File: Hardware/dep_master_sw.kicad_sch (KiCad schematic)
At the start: 11 parts, among them Q5 BSZ025N04LS, Q6 BSZ025N04LS, U8 LM74810

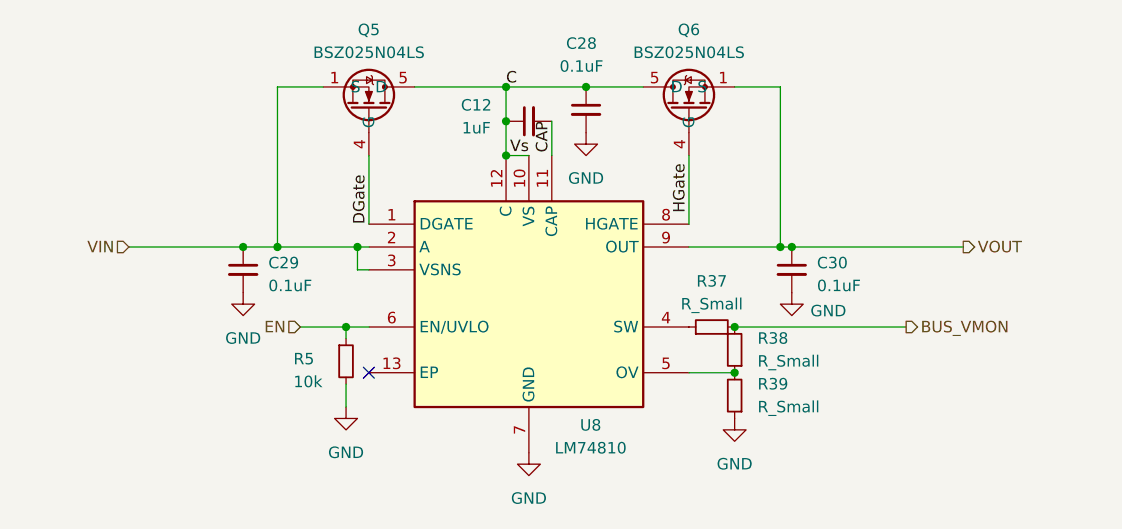
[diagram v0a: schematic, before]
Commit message: TVS diode and sized resistor ladder
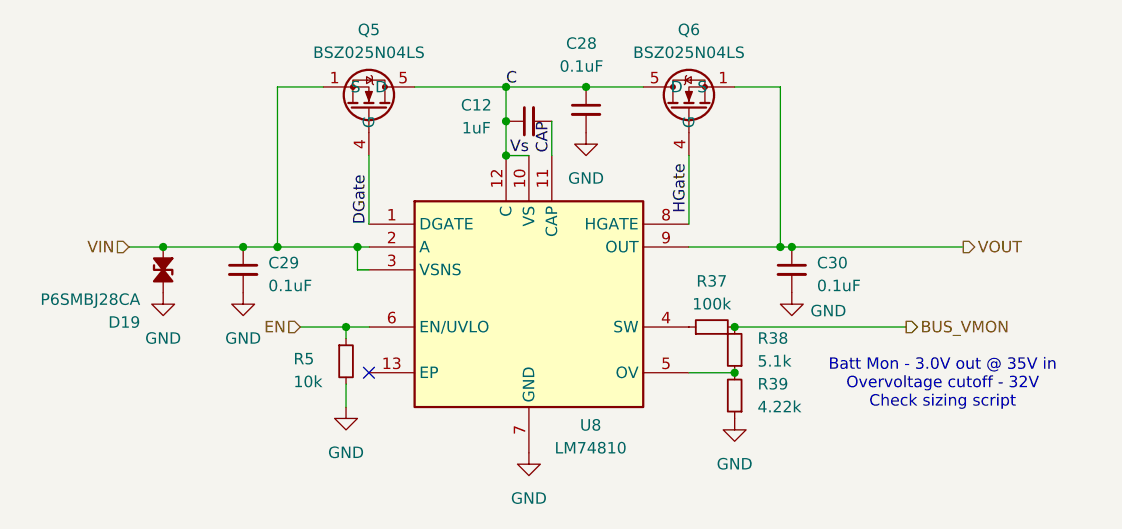
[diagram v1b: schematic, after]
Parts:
- added D19: P6SMBJ28CA, Diode_SMD:D_SMA, symbol Device:D_TVS_Small_Filled
- R37: value R_Small -> 100k
- R38: value R_Small -> 5.1k
- R39: value R_Small -> 4.22k
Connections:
- net GND: now also D19.2 (A2)
- net VIN: now also D19.1 (A1)
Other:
- note added: "Batt Mon - 3.0V out @ 35V in Overvoltage cutoff - 32V Check sizing script"
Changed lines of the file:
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@@
+		(color 0 0 0 0)
+	)
+	(junction
+		(at 99.06 62.23)
+		(diameter 0)
 		(color 0 0 0 0)
 	)
@@
 	(wire
 		(pts
+			(xy 99.06 62.23) (xy 107.95 62.23)
+		)
+		(stroke
+			(width 0)
+			(type default)
+		)
+	)
+	(wire
+		(pts
 			(xy 157.48 52.07) (xy 157.48 59.69)
 		)
@@
 	(wire
 		(pts
-			(xy 95.25 62.23) (xy 107.95 62.23)
+			(xy 95.25 62.23) (xy 99.06 62.23)
 		)
 		(stroke
@@
 			(width 0)
 			(type default)
+		)
+	)
+	(text "Batt Mon - 3.0V out @ 35V in\nOvervoltage cutoff - 32V\nCheck sizing script"
+		(exclude_from_sim no)
+		(at 185.674 77.47 0)
+		(effects
+			(font
+				(size 1.27 1.27)
+			)
 		)
 	)
@@
 	)
 	(symbol
+		(lib_id "power:GND")
+		(at 99.06 67.31 0)
+		(unit 1)
+		(exclude_from_sim no)
+		(in_bom yes)
+		(on_board yes)
+		(dnp no)
+		(fields_autoplaced yes)
+		(property "Reference" "#PWR077"
+			(at 99.06 73.66 0)
+			(effects
+				(font
+					(size 1.27 1.27)
+				)
+				(hide yes)
+			)
+		)
+		(property "Value" "GND"
+			(at 99.06 72.39 0)
+			(effects
+				(font
+					(size 1.27 1.27)
+				)
+			)
+		)
+		(property "Footprint" ""
+			(at 99.06 67.31 0)
+			(effects
+				(font
+					(size 1.27 1.27)
+				)
+				(hide yes)
+			)
+		)
+		(property "Datasheet" ""
+			(at 99.06 67.31 0)
+			(effects
+				(font
+					(size 1.27 1.27)
+				)
+				(hide yes)
+			)
+		)
+		(property "Description" "Power symbol creates a global label with name \"GND\" , ground"
+			(at 99.06 67.31 0)
+			(effects
+				(font
+					(size 1.27 1.27)
+				)
+				(hide yes)
+			)
+		)
+		(pin "1"
+		)
+		(instances
+			(project "flintandsteel"
+				(path "/7db990e4-92e1-4f99-b4d2-435bbec1ba83/62d4ea8d-f53f-40d2-8855-48df78fda698"
+					(reference "#PWR077")
+					(unit 1)
+				)
+			)
+		)
+	)
+	(symbol
 		(lib_id "Device:R_Small")
 		(at 160.02 71.12 90)
@@
 			)
 		)
-		(property "Value" "R_Small"
+		(property "Value" "100k"
 			(at 160.02 68.58 90)
 			(effects
@@
 			)
 		)
-		(property "Value" "R_Small"
+		(property "Value" "5.1k"
 			(at 165.1 74.9299 0)
 			(effects
@@
 			)
 		)
-		(property "Value" "R_Small"
+		(property "Value" "4.22k"
 			(at 165.1 80.0099 0)
 			(effects
@@
 					(unit 1)
 				)
+			)
+		)
+	)
+	(symbol
+		(lib_id "Device:D_TVS_Small_Filled")
+		(at 99.06 64.77 270)
+		(unit 1)
+		(exclude_from_sim no)
+		(in_bom yes)
+		(on_board yes)
+		(dnp no)
+		(property "Reference" "D19"
+			(at 96.52 70.612 90)
+			(effects
+				(font
+					(size 1.27 1.27)
+				)
+				(justify right)
+			)
+		)
+		(property "Value" "P6SMBJ28CA"
+			(at 96.52 68.072 90)
+			(effects
+				(font
+					(size 1.27 1.27)
+				)
+				(justify right)
+			)
+		)
+		(property "Footprint" "Diode_SMD:D_SMA"
+			(at 99.06 64.77 0)
+			(effects
+				(font
+					(size 1.27 1.27)
+				)
+				(hide yes)
+			)
+		)
+		(property "Datasheet" "~"
+			(at 99.06 64.77 0)
+			(effects
+				(font
+					(size 1.27 1.27)
+				)
+				(hide yes)
+			)
+		)
+		(property "Description" "Bidirectional transient-voltage-suppression diode, small symbol, filled shape"
+			(at 99.06 64.77 0)
+			(effects
+				(font
+					(size 1.27 1.27)
+				)
+				(hide yes)
+			)
+		)
+		(pin "2"
+		)
+		(pin "1"
+		)
+		(instances
+			(project ""
+				(path "/7db990e4-92e1-4f99-b4d2-435bbec1ba83/62d4ea8d-f53f-40d2-8855-48df78fda698"
+					(reference "D19")
+					(unit 1)
+				)

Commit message: tidied up schematic and bom
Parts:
- C301: renamed from C29; value 0.1uF -> 100nF
- C303: renamed from C28; value 0.1uF -> 100nF
- C304: renamed from C30; value 0.1uF -> 100nF
- R301: renamed from R5; value 10k -> 10kΩ
- R302: renamed from R37; value 100k -> 100kΩ
- R303: renamed from R38; value 5.1k -> 5.1kΩ
- R304: renamed from R39; value 4.22k -> 4.22kΩ
- renumbered C12 to C302, D19 to D301, Q5 to Q301, Q6 to Q302, U8 to U301
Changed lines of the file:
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@@
 		(on_board yes)
 		(dnp no)
-		(property "Reference" "C29"
+		(property "Reference" "C301"
 			(at 110.744 64.008 0)
 			(effects
@@
 			)
 		)
-		(property "Value" "0.1uF"
+		(property "Value" "100nF"
 			(at 110.744 66.548 0)
 			(effects
@@
 		)
 		(instances
-			(project ""
-				(path "/7db990e4-92e1-4f99-b4d2-435bbec1ba83/62d4ea8d-f53f-40d2-8855-48df78fda698"
-					(reference "C29")
+			(project "flintandsteel"
+				(path "/7db990e4-92e1-4f99-b4d2-435bbec1ba83/62d4ea8d-f53f-40d2-8855-48df78fda698"
+					(reference "C301")
 					(unit 1)
 				)
@@
 		(dnp no)
 		(fields_autoplaced yes)
-		(property "Reference" "#PWR072"
+		(property "Reference" "#PWR0306"
 			(at 162.56 87.63 0)
 			(effects
@@
 			(project "flintandsteel"
 				(path "/7db990e4-92e1-4f99-b4d2-435bbec1ba83/62d4ea8d-f53f-40d2-8855-48df78fda698"
-					(reference "#PWR072")
+					(reference "#PWR0306")
 					(unit 1)
 				)
@@
 		(dnp no)
 		(fields_autoplaced yes)
-		(property "Reference" "#PWR070"
+		(property "Reference" "#PWR0302"
 			(at 107.95 73.66 0)
 			(effects
@@
 			(project "flintandsteel"
 				(path "/7db990e4-92e1-4f99-b4d2-435bbec1ba83/62d4ea8d-f53f-40d2-8855-48df78fda698"
-					(reference "#PWR070")
+					(reference "#PWR0302")
 					(unit 1)
 				)
@@
 		(on_board yes)
 		(dnp no)
-		(property "Reference" "C12"
+		(property "Reference" "C302"
 			(at 133.858 46.482 90)
 			(effects
@@
 		)
 		(instances
-			(project ""
-				(path "/7db990e4-92e1-4f99-b4d2-435bbec1ba83/62d4ea8d-f53f-40d2-8855-48df78fda698"
-					(reference "C12")
+			(project "flintandsteel"
+				(path "/7db990e4-92e1-4f99-b4d2-435bbec1ba83/62d4ea8d-f53f-40d2-8855-48df78fda698"
+					(reference "C302")
 					(unit 1)
 				)
@@
 		(on_board yes)
 		(dnp no)
-		(property "Reference" "C28"
+		(property "Reference" "C303"
 			(at 145.542 39.624 0)
 			(effects
@@
 			)
 		)
-		(property "Value" "0.1uF"
+		(property "Value" "100nF"
 			(at 145.542 42.164 0)
 			(effects
@@
 			(project "flintandsteel"
 				(path "/7db990e4-92e1-4f99-b4d2-435bbec1ba83/62d4ea8d-f53f-40d2-8855-48df78fda698"
-					(reference "C28")
+					(reference "C303")
 					(unit 1)
 				)
@@
 		(dnp no)
 		(fields_autoplaced yes)
-		(property "Reference" "Q6"
+		(property "Reference" "Q302"
 			(at 157.48 38.1 90)
 			(effects
@@
 		)
 		(instances
-			(project ""
-				(path "/7db990e4-92e1-4f99-b4d2-435bbec1ba83/62d4ea8d-f53f-40d2-8855-48df78fda698"
-					(reference "Q6")
+			(project "flintandsteel"
+				(path "/7db990e4-92e1-4f99-b4d2-435bbec1ba83/62d4ea8d-f53f-40d2-8855-48df78fda698"
+					(reference "Q302")
 					(unit 1)
 				)
@@
 		(dnp no)
 		(fields_autoplaced yes)
-		(property "Reference" "#PWR077"
+		(property "Reference" "#PWR0301"
 			(at 99.06 73.66 0)
 			(effects
@@
 			(project "flintandsteel"
 				(path "/7db990e4-92e1-4f99-b4d2-435bbec1ba83/62d4ea8d-f53f-40d2-8855-48df78fda698"
-					(reference "#PWR077")
+					(reference "#PWR0301")
 					(unit 1)
 				)
@@
 		(dnp no)
 		(fields_autoplaced yes)
-		(property "Reference" "R37"
+		(property "Reference" "R302"
 			(at 160.02 66.04 90)
 			(effects
@@
 			)
 		)
-		(property "Value" "100k"
+		(property "Value" "100kΩ"
 			(at 160.02 68.58 90)
 			(effects
@@
 		)
 		(instances
-			(project ""
-				(path "/7db990e4-92e1-4f99-b4d2-435bbec1ba83/62d4ea8d-f53f-40d2-8855-48df78fda698"
-					(reference "R37")
+			(project "flintandsteel"
+				(path "/7db990e4-92e1-4f99-b4d2-435bbec1ba83/62d4ea8d-f53f-40d2-8855-48df78fda698"
+					(reference "R302")
 					(unit 1)
 				)
@@
 		(on_board yes)
 		(dnp no)
-		(property "Reference" "C30"
+		(property "Reference" "C304"
 			(at 171.704 64.008 0)
 			(effects
@@
 			)
 		)
-		(property "Value" "0.1uF"
+		(property "Value" "100nF"
 			(at 171.704 66.548 0)
 			(effects
@@
 			(project "flintandsteel"
 				(path "/7db990e4-92e1-4f99-b4d2-435bbec1ba83/62d4ea8d-f53f-40d2-8855-48df78fda698"
-					(reference "C30")
+					(reference "C304")
 					(unit 1)
 				)
@@
 		(dnp no)
 		(fields_autoplaced yes)
-		(property "Reference" "R38"
+		(property "Reference" "R303"
 			(at 165.1 72.3899 0)
 			(effects
@@
 			)
 		)
-		(property "Value" "5.1k"
+		(property "Value" "5.1kΩ"
 			(at 165.1 74.9299 0)
 			(effects
@@
 			(project "flintandsteel"
 				(path "/7db990e4-92e1-4f99-b4d2-435bbec1ba83/62d4ea8d-f53f-40d2-8855-48df78fda698"
-					(reference "R38")
+					(reference "R303")
 					(unit 1)
 				)
@@
 		(dnp no)
 		(fields_autoplaced yes)
-		(property "Reference" "#PWR069"
+		(property "Reference" "#PWR0305"
 			(at 146.05 55.88 0)
 			(effects
@@
 			(project "flintandsteel"
 				(path "/7db990e4-92e1-4f99-b4d2-435bbec1ba83/62d4ea8d-f53f-40d2-8855-48df78fda698"
-					(reference "#PWR069")
+					(reference "#PWR0305")
 					(unit 1)
 				)
@@
 		(dnp no)
 		(fields_autoplaced yes)
-		(property "Reference" "#PWR015"
+		(property "Reference" "#PWR0303"
 			(at 119.38 86.36 0)
 			(effects
@@
 		)
 		(instances
-			(project ""
-				(path "/7db990e4-92e1-4f99-b4d2-435bbec1ba83/62d4ea8d-f53f-40d2-8855-48df78fda698"
-					(reference "#PWR015")
+			(project "flintandsteel"
+				(path "/7db990e4-92e1-4f99-b4d2-435bbec1ba83/62d4ea8d-f53f-40d2-8855-48df78fda698"
+					(reference "#PWR0303")
 					(unit 1)
 				)
@@
 		(on_board yes)
 		(dnp no)
-		(property "Reference" "U8"
+		(property "Reference" "U301"
 			(at 146.558 82.042 0)
 			(effects
@@
 		)
 		(instances
-			(project ""
-				(path "/7db990e4-92e1-4f99-b4d2-435bbec1ba83/62d4ea8d-f53f-40d2-8855-48df78fda698"
-					(reference "U8")
+			(project "flintandsteel"
+				(path "/7db990e4-92e1-4f99-b4d2-435bbec1ba83/62d4ea8d-f53f-40d2-8855-48df78fda698"
+					(reference "U301")
 					(unit 1)
 				)
@@
 		(dnp no)
 		(fields_autoplaced yes)
-		(property "Reference" "R39"
+		(property "Reference" "R304"
 			(at 165.1 77.4699 0)
 			(effects
@@
 			)
 		)
-		(property "Value" "4.22k"
+		(property "Value" "4.22kΩ"
 			(at 165.1 80.0099 0)
 			(effects
@@
 			(project "flintandsteel"
 				(path "/7db990e4-92e1-4f99-b4d2-435bbec1ba83/62d4ea8d-f53f-40d2-8855-48df78fda698"
-					(reference "R39")
+					(reference "R304")
 					(unit 1)
 				)
@@
 		(on_board yes)
 		(dnp no)
-		(property "Reference" "R5"
+		(property "Reference" "R301"
 			(at 113.538 74.676 0)
 			(effects
@@
 			)
 		)
-		(property "Value" "10k"
+		(property "Value" "10kΩ"
 			(at 113.538 77.216 0)
 			(effects
@@
 		)
 		(instances
-			(project ""
-				(path "/7db990e4-92e1-4f99-b4d2-435bbec1ba83/62d4ea8d-f53f-40d2-8855-48df78fda698"
-					(reference "R5")
+			(project "flintandsteel"
+				(path "/7db990e4-92e1-4f99-b4d2-435bbec1ba83/62d4ea8d-f53f-40d2-8855-48df78fda698"
+					(reference "R301")
 					(unit 1)
 				)
@@
 		(on_board yes)
 		(dnp no)
-		(property "Reference" "#PWR071"
+		(property "Reference" "#PWR0307"
 			(at 168.91 73.66 0)
 			(effects
@@
 			(project "flintandsteel"
 				(path "/7db990e4-92e1-4f99-b4d2-435bbec1ba83/62d4ea8d-f53f-40d2-8855-48df78fda698"
-					(reference "#PWR071")
+					(reference "#PWR0307")
 					(unit 1)
 				)
@@
 		(on_board yes)
 		(dnp no)
-		(property "Reference" "Q5"
+		(property "Reference" "Q301"
 			(at 121.92 38.1 90)
 			(effects
@@
 			(project "flintandsteel"
 				(path "/7db990e4-92e1-4f99-b4d2-435bbec1ba83/62d4ea8d-f53f-40d2-8855-48df78fda698"
-					(reference "Q5")
+					(reference "Q301")
 					(unit 1)
 				)
@@
 		(dnp no)
 		(fields_autoplaced yes)
-		(property "Reference" "#PWR09"
+		(property "Reference" "#PWR0304"
 			(at 139.7 91.44 0)
 			(effects
@@
 			(project "flintandsteel"
 				(path "/7db990e4-92e1-4f99-b4d2-435bbec1ba83/62d4ea8d-f53f-40d2-8855-48df78fda698"
-					(reference "#PWR09")
+					(reference "#PWR0304")
 					(unit 1)
 				)
@@
 		(on_board yes)
 		(dnp no)
-		(property "Reference" "D19"
+		(property "Reference" "D301"
 			(at 96.52 70.612 90)
 			(effects
@@
 		)
 		(instances
-			(project ""
-				(path "/7db990e4-92e1-4f99-b4d2-435bbec1ba83/62d4ea8d-f53f-40d2-8855-48df78fda698"
-					(reference "D19")
-					(unit 1)
-				)
+			(project "flintandsteel"
+				(path "/7db990e4-92e1-4f99-b4d2-435bbec1ba83/62d4ea8d-f53f-40d2-8855-48df78fda698"
+					(reference "D301")
+					(unit 1)
+				)
